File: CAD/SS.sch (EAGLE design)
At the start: 131 parts, among them Q1 SN74AHC-NOR, Q2 UMD5N, Q3 MIC5205, Q4 SN74AHC-AND, Q5 BFP460, Q6 TCR1HF50, T1 MMBTRA104SS, X1 ANTENNA, X2 RADIO, X3 INP, X4 AMP-O, X5 BPF-O

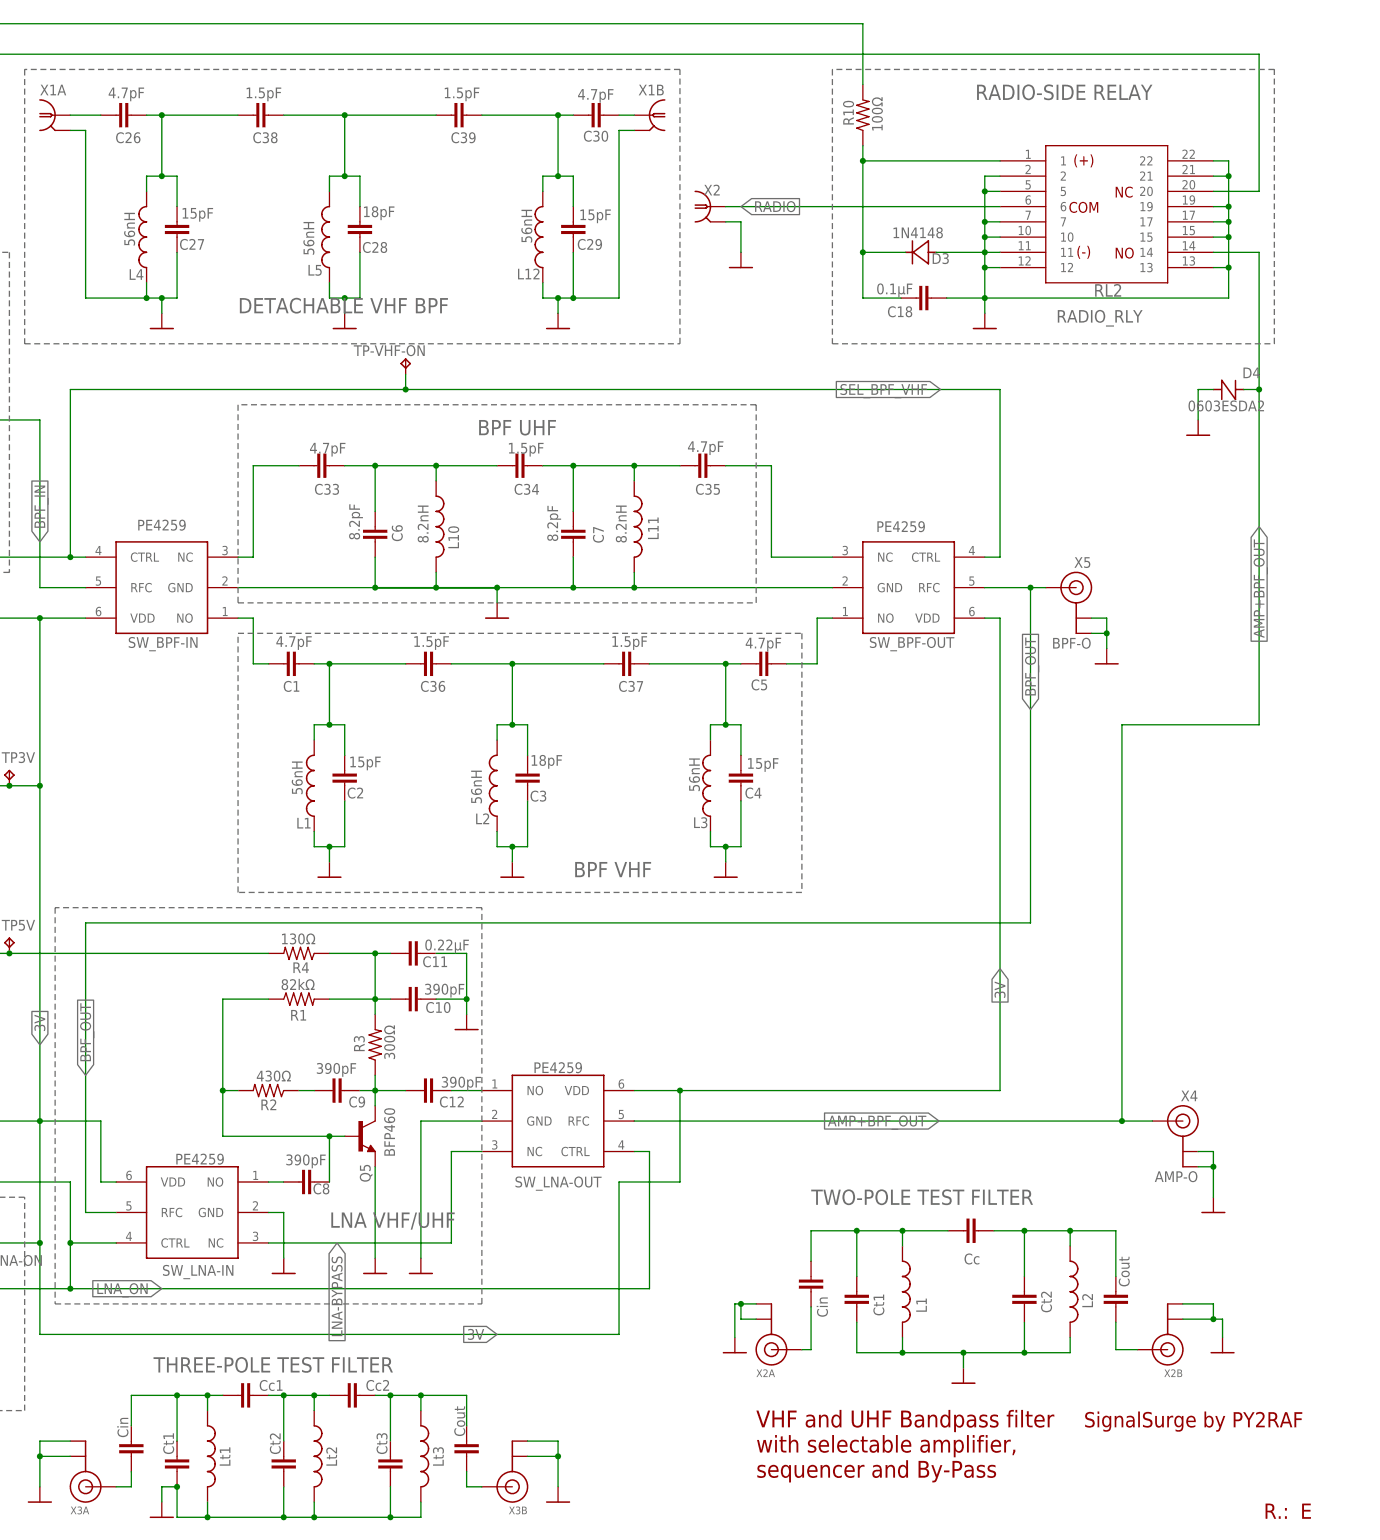
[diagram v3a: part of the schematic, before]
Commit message: Rev. E bug fixes
* Added new VHF filter test figures
* Fixed a gross error where a via shorted the VHF BPF final coupling stage
* Removed ground pad on inductors at the detachable VHF BPF.
* Improved the radio signal trace at the first RF relay input.
* Updated component values for the 3-pole VHF filter (*in vivo* performed differently than the *in vitro*)
* Updated BOM
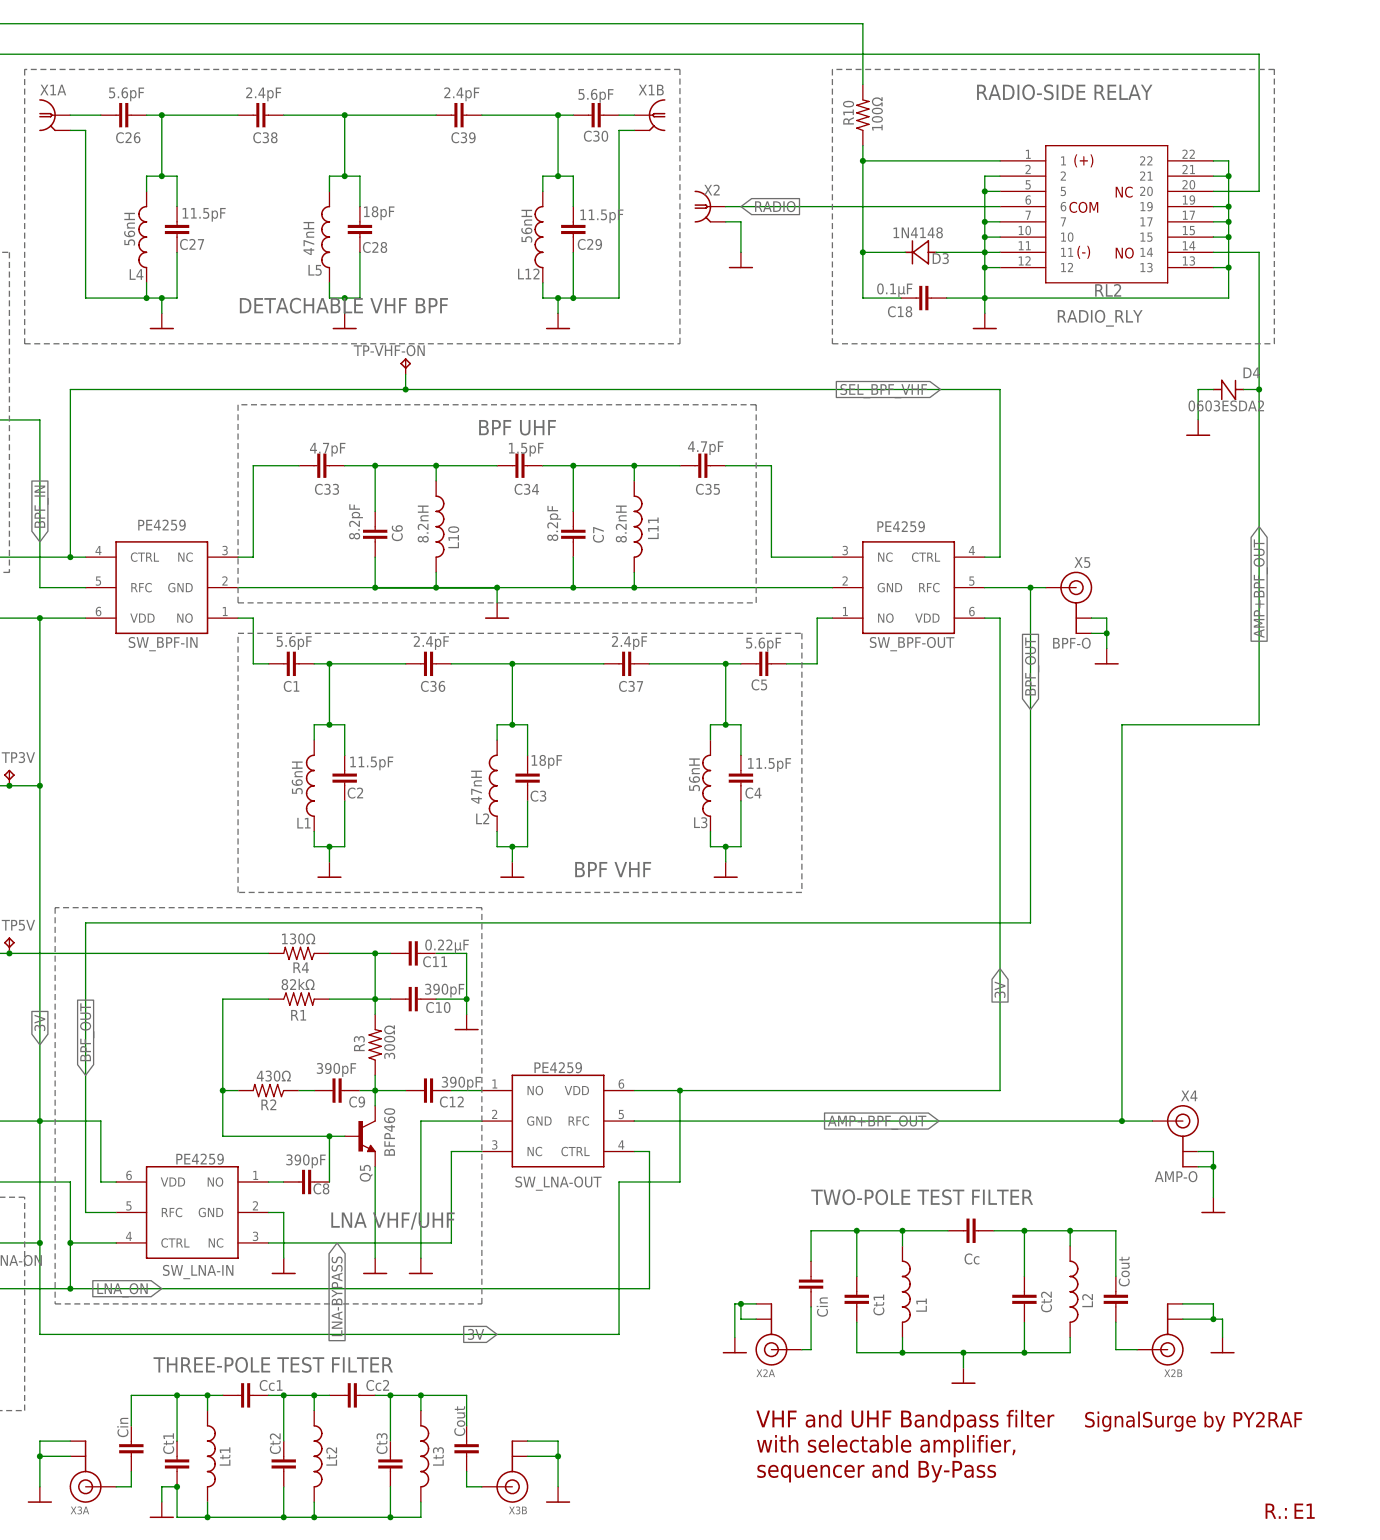
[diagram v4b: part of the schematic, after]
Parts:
- C1, C26, C30, C5: value 4.7pF -> 5.6pF
- C2, C27, C29, C4: value 15pF -> 11.5pF
- C36, C37, C38, C39: value 1.5pF -> 2.4pF
- L2, L5: value 56nH -> 47nH
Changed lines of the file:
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@@
 <schematic xreflabel="%F%N/%S.%C%R" xrefpart="/%S.%C%R">
 <attributes>
-<attribute name="REVISION" value="E"/>
+<attribute name="REVISION" value="E1"/>
 </attributes>
 <variantdefs>
@@
 <part name="FRAME1" library="frames" library_urn="urn:adsk.eagle:library:229" deviceset="A3L-LOC" device=""/>
 <part name="L1" library="aarf" deviceset="L-0805" device="" value="56nH"/>
-<part name="L2" library="aarf" deviceset="L-0805" device="" value="56nH"/>
+<part name="L2" library="aarf" deviceset="L-0805" device="" value="47nH"/>
 <part name="L3" library="aarf" deviceset="L-0805" device="" value="56nH"/>
-<part name="C1" library="aarf" deviceset="C-0805" device="" value="4.7pF"/>
-<part name="C2" library="aarf" deviceset="C-0805" device="" value="15pF"/>
+<part name="C1" library="aarf" deviceset="C-0805" device="" value="5.6pF"/>
+<part name="C2" library="aarf" deviceset="C-0805" device="" value="11.5pF"/>
 <part name="C34" library="aarf" deviceset="C-0805" device="" value="1.5pF"/>
 <part name="C35" library="aarf" deviceset="C-0805" device="" value="4.7pF"/>
@@
 <part name="3V" library="aarf" deviceset="JUMPER-1" device="" value="3V"/>
 <part name="C3" library="aarf" deviceset="C-0805" device="" value="18pF"/>
-<part name="C4" library="aarf" deviceset="C-0805" device="" value="15pF"/>
-<part name="C5" library="aarf" deviceset="C-0805" device="" value="4.7pF"/>
+<part name="C4" library="aarf" deviceset="C-0805" device="" value="11.5pF"/>
+<part name="C5" library="aarf" deviceset="C-0805" device="" value="5.6pF"/>
 <part name="GND12" library="supply1" library_urn="urn:adsk.eagle:library:371" deviceset="GND" device=""/>
 <part name="GND28" library="supply1" library_urn="urn:adsk.eagle:library:371" deviceset="GND" device=""/>
@@
 <part name="GND38" library="supply1" library_urn="urn:adsk.eagle:library:371" deviceset="GND" device=""/>
 <part name="L4" library="aarf" deviceset="L-0805" device="" value="56nH"/>
-<part name="L5" library="aarf" deviceset="L-0805" device="" value="56nH"/>
+<part name="L5" library="aarf" deviceset="L-0805" device="" value="47nH"/>
 <part name="L12" library="aarf" deviceset="L-0805" device="" value="56nH"/>
-<part name="C26" library="aarf" deviceset="C-0805" device="" value="4.7pF"/>
-<part name="C27" library="aarf" deviceset="C-0805" device="" value="15pF"/>
+<part name="C26" library="aarf" deviceset="C-0805" device="" value="5.6pF"/>
+<part name="C27" library="aarf" deviceset="C-0805" device="" value="11.5pF"/>
 <part name="C28" library="aarf" deviceset="C-0805" device="" value="18pF"/>
-<part name="C29" library="aarf" deviceset="C-0805" device="" value="15pF"/>
-<part name="C30" library="aarf" deviceset="C-0805" device="" value="4.7pF"/>
+<part name="C29" library="aarf" deviceset="C-0805" device="" value="11.5pF"/>
+<part name="C30" library="aarf" deviceset="C-0805" device="" value="5.6pF"/>
 <part name="GND35" library="supply1" library_urn="urn:adsk.eagle:library:371" deviceset="GND" device=""/>
 <part name="GND36" library="supply1" library_urn="urn:adsk.eagle:library:371" deviceset="GND" device=""/>
@@
 <part name="R17" library="aarf" deviceset="R-1206" device="" value="10kΩ"/>
 <part name="GND44" library="supply1" library_urn="urn:adsk.eagle:library:371" deviceset="GND" device=""/>
-<part name="C36" library="aarf" deviceset="C-0805" device="" value="1.5pF"/>
-<part name="C37" library="aarf" deviceset="C-0805" device="" value="1.5pF"/>
-<part name="C38" library="aarf" deviceset="C-0805" device="" value="1.5pF"/>
-<part name="C39" library="aarf" deviceset="C-0805" device="" value="1.5pF"/>
+<part name="C36" library="aarf" deviceset="C-0805" device="" value="2.4pF"/>
+<part name="C37" library="aarf" deviceset="C-0805" device="" value="2.4pF"/>
+<part name="C38" library="aarf" deviceset="C-0805" device="" value="2.4pF"/>
+<part name="C39" library="aarf" deviceset="C-0805" device="" value="2.4pF"/>
 <part name="X3A" library="adafruit" deviceset="ANTENNA_U.FL" device=""/>
 <part name="C40" library="aarf" deviceset="C-0805" device="" value="Cin"/>
@@
 <text x="344.17" y="32.766" size="2.54" layer="94">SignalSurge by PY2RAF</text>
 <text x="374.142" y="17.526" size="2.54" layer="94">R.:</text>
-<text x="380.238" y="17.526" size="2.54" layer="94">&gt;REVISION</text>
+<text x="378.968" y="17.526" size="2.54" layer="94">&gt;REVISION</text>
 <text x="289.56" y="35.56" size="2.794" layer="94" align="top-left">VHF and UHF Bandpass filter
 with selectable amplifier,

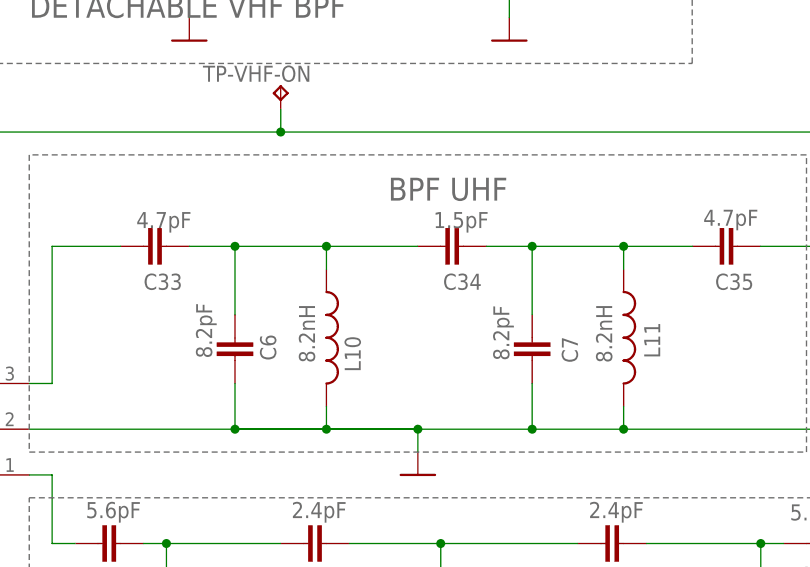
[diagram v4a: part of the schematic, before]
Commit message: UHF filter improvements and testing figures.
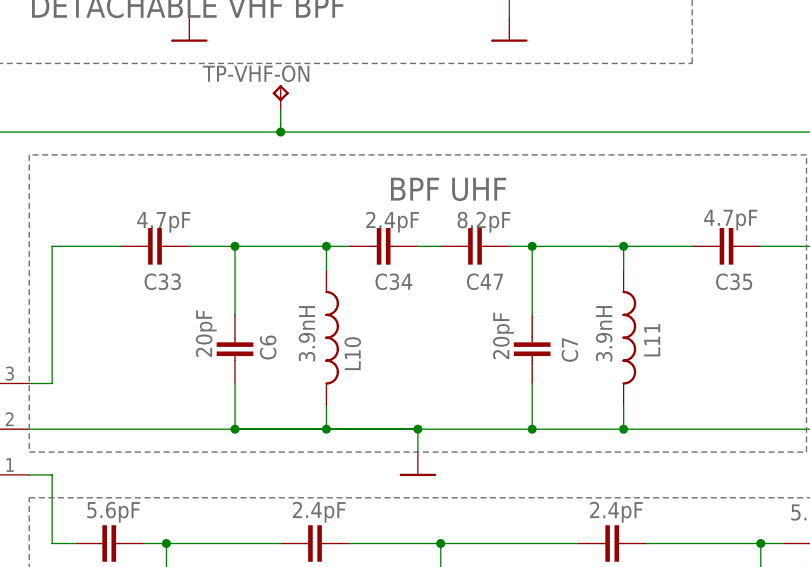
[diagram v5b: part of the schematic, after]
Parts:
- added C47: 8.2pF, aarf:C-0805
- C34: value 1.5pF -> 2.4pF
- C6, C7: value 8.2pF -> 20pF
- L10, L11: value 8.2nH -> 3.9nH
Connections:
- new net 1.86PF: C34.2, C47.1
- net UHF-P2: now also C47.2; no longer C34.2
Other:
- moved on the sheet: C34
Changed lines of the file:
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@@
 <part name="C1" library="aarf" deviceset="C-0805" device="" value="5.6pF"/>
 <part name="C2" library="aarf" deviceset="C-0805" device="" value="11.5pF"/>
-<part name="C34" library="aarf" deviceset="C-0805" device="" value="1.5pF"/>
+<part name="C34" library="aarf" deviceset="C-0805" device="" value="2.4pF"/>
 <part name="C35" library="aarf" deviceset="C-0805" device="" value="4.7pF"/>
-<part name="C6" library="aarf" deviceset="C-0805" device="" value="8.2pF"/>
-<part name="C7" library="aarf" deviceset="C-0805" device="" value="8.2pF"/>
+<part name="C6" library="aarf" deviceset="C-0805" device="" value="20pF"/>
+<part name="C7" library="aarf" deviceset="C-0805" device="" value="20pF"/>
 <part name="C8" library="aarf" deviceset="C-0805" device="" value="390pF"/>
 <part name="R1" library="aarf" deviceset="R-1206" device="" value="82kΩ"/>
@@
 <part name="GND19" library="supply1" library_urn="urn:adsk.eagle:library:371" deviceset="GND" device=""/>
 <part name="C33" library="aarf" deviceset="C-0805" device="" value="4.7pF"/>
-<part name="L10" library="aarf" deviceset="L-0805" device="" value="8.2nH"/>
-<part name="L11" library="aarf" deviceset="L-0805" device="" value="8.2nH"/>
+<part name="L10" library="aarf" deviceset="L-0805" device="" value="3.9nH"/>
+<part name="L11" library="aarf" deviceset="L-0805" device="" value="3.9nH"/>
 <part name="GND16" library="supply1" library_urn="urn:adsk.eagle:library:371" deviceset="GND" device=""/>
 <part name="GND18" library="supply1" library_urn="urn:adsk.eagle:library:371" deviceset="GND" device=""/>
@@
 <part name="GND21" library="supply1" library_urn="urn:adsk.eagle:library:371" deviceset="GND" device=""/>
 <part name="Q3" library="aarf" deviceset="MIC5205" device="" package3d_urn="urn:adsk.eagle:package:2406/1"/>
+<part name="C47" library="aarf" deviceset="C-0805" device="" value="8.2pF"/>
 </parts>
 <sheets>
@@
 <attribute name="VALUE" x="221.664" y="142.779" size="1.778" layer="96"/>
 </instance>
-<instance part="C34" gate="G$1" x="248.92" y="193.04" smashed="yes" rot="R90">
-<attribute name="NAME" x="253.492" y="189.992" size="1.778" layer="95" rot="R180"/>
-<attribute name="VALUE" x="254.254" y="196.85" size="1.778" layer="96" rot="R180"/>
+<instance part="C34" gate="G$1" x="241.3" y="193.04" smashed="yes" rot="R90">
+<attribute name="NAME" x="245.872" y="189.992" size="1.778" layer="95" rot="R180"/>
+<attribute name="VALUE" x="246.634" y="196.85" size="1.778" layer="96" rot="R180"/>
 </instance>
 <instance part="C35" gate="G$1" x="279.4" y="193.04" smashed="yes" rot="R90">
@@
 <attribute name="NAME" x="122.174" y="135.128" size="1.778" layer="95"/>
 <attribute name="VALUE" x="119.38" y="132.08" size="1.778" layer="96"/>
+</instance>
+<instance part="C47" gate="G$1" x="251.46" y="193.04" smashed="yes" rot="R90">
+<attribute name="NAME" x="256.032" y="189.992" size="1.778" layer="95" rot="R180"/>
+<attribute name="VALUE" x="256.794" y="196.85" size="1.778" layer="96" rot="R180"/>
 </instance>
 </instances>
@@
 <segment>
 <pinref part="C33" gate="G$1" pin="2"/>
-<pinref part="C34" gate="G$1" pin="1"/>
 <wire x1="220.98" y1="193.04" x2="226.06" y2="193.04" width="0.1524" layer="91"/>
 <pinref part="C6" gate="G$1" pin="2"/>
 <wire x1="226.06" y1="193.04" x2="236.22" y2="193.04" width="0.1524" layer="91"/>
-<wire x1="236.22" y1="193.04" x2="246.38" y2="193.04" width="0.1524" layer="91"/>
 <wire x1="226.06" y1="185.42" x2="226.06" y2="193.04" width="0.1524" layer="91"/>
 <junction x="226.06" y="193.04"/>
 <pinref part="L10" gate="G$1" pin="1"/>
 <wire x1="236.22" y1="190.5" x2="236.22" y2="193.04" width="0.1524" layer="91"/>
+<pinref part="C34" gate="G$1" pin="1"/>
+<wire x1="236.22" y1="193.04" x2="238.76" y2="193.04" width="0.1524" layer="91"/>
 <junction x="236.22" y="193.04"/>
 </segment>
@@
 <net name="UHF-P2" class="1">
 <segment>
-<pinref part="C34" gate="G$1" pin="2"/>
 <pinref part="C35" gate="G$1" pin="1"/>
-<wire x1="254" y1="193.04" x2="259.08" y2="193.04" width="0.1524" layer="91"/>
 <pinref part="C7" gate="G$1" pin="2"/>
 <wire x1="259.08" y1="193.04" x2="269.24" y2="193.04" width="0.1524" layer="91"/>
 <wire x1="269.24" y1="193.04" x2="276.86" y2="193.04" width="0.1524" layer="91"/>
 <wire x1="259.08" y1="185.42" x2="259.08" y2="193.04" width="0.1524" layer="91"/>
-<junction x="259.08" y="193.04"/>
 <pinref part="L11" gate="G$1" pin="1"/>
 <wire x1="269.24" y1="190.5" x2="269.24" y2="193.04" width="0.1524" layer="91"/>
 <junction x="269.24" y="193.04"/>
+<pinref part="C47" gate="G$1" pin="2"/>
+<wire x1="256.54" y1="193.04" x2="259.08" y2="193.04" width="0.1524" layer="91"/>
+<junction x="259.08" y="193.04"/>
 </segment>
 </net>
@@
 </segment>
 </net>
+<net name="1.86PF" class="1">
+<segment>
+<pinref part="C34" gate="G$1" pin="2"/>
+<pinref part="C47" gate="G$1" pin="1"/>
+<wire x1="246.38" y1="193.04" x2="248.92" y2="193.04" width="0.1524" layer="91"/>
+</segment>
+</net>
